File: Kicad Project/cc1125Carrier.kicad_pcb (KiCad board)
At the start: 2 copper layers, 65.9 x 78 mm, 7 parts, among them J1 TFM-110-02-SM-D-A-K-TR, J2 TFM-110-02-SM-D-A-K-TR, J3 Jumper Block, J4 Conn_01x06, U1 YAAJ_WeAct_BlackPill_Part_Lik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

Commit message: add STM project & re-arrange to include it
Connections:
- U1 pad 23: NRST -> unconnected-(U1-Pad23)
- U1 pad 29: unconnected-(U1-Pad29) -> NRST
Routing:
- net NRST: track 45.9 -> 38.1 mm
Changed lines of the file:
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@@
   (net 43 "unconnected-(U1-Pad9)")
   (net 44 "unconnected-(U1-Pad10)")
-  (net 45 "unconnected-(U1-Pad29)")
+  (net 45 "unconnected-(U1-Pad23)")
   (net 46 "unconnected-(U1-Pad16)")
   (net 47 "unconnected-(U1-Pad24)")
@@
       (net 50 "unconnected-(U1-Pad22)") (pinfunction "PC13") (pintype "bidirectional"))
     (pad "23" thru_hole circle locked (at 15.24 43.18 90) (size 1.7 1.7) (drill 1) (layers *.Cu *.Mask)
-      (net 21 "NRST") (pinfunction "PC14") (pintype "bidirectional"))
+      (net 45 "unconnected-(U1-Pad23)") (pinfunction "PC14") (pintype "bidirectional"))
     (pad "24" thru_hole circle locked (at 15.24 40.64 90) (size 1.7 1.7) (drill 1) (layers *.Cu *.Mask)
       (net 47 "unconnected-(U1-Pad24)") (pinfunction "PC15") (pintype "bidirectional"))
@@
       (net 10 "GPIO0") (pinfunction "PA2") (pintype "bidirectional"))
     (pad "29" thru_hole circle locked (at 15.24 27.94 90) (size 1.7 1.7) (drill 1) (layers *.Cu *.Mask)
-      (net 45 "unconnected-(U1-Pad29)") (pinfunction "PA3") (pintype "bidirectional"))
+      (net 21 "NRST") (pinfunction "PA3") (pintype "bidirectional"))
     (pad "30" thru_hole circle locked (at 15.24 25.4 90) (size 1.7 1.7) (drill 1) (layers *.Cu *.Mask)
       (net 14 "NSS") (pinfunction "PA4") (pintype "bidirectional"))
@@
   (segment (start 125 94.72) (end 125.005 94.725) (width 0.25) (layer "F.Cu") (net 21))
   (via (at 125 94.72) (size 0.8) (drill 0.4) (layers "F.Cu" "B.Cu") (net 21))
-  (segment (start 140.39 97.73) (end 136.75 94.09) (width 0.25) (layer "B.Cu") (net 21))
-  (segment (start 125.63 94.09) (end 125 94.72) (width 0.25) (layer "B.Cu") (net 21))
-  (segment (start 136.75 94.09) (end 125.63 94.09) (width 0.25) (layer "B.Cu") (net 21))
-  (segment (start 140.39 113.19) (end 140.39 97.73) (width 0.25) (layer "B.Cu") (net 21))
-  (segment (start 133.76 119.82) (end 140.39 113.19) (width 0.25) (layer "B.Cu") (net 21))
+  (segment (start 116.74 102.98) (end 125 94.72) (width 0.25) (layer "B.Cu") (net 21))
+  (segment (start 121.001988 108.18) (end 116.97 108.18) (width 0.25) (layer "B.Cu") (net 21))
+  (segment (start 118.52 119.82) (end 118.52 114.69) (width 0.25) (layer "B.Cu") (net 21))
+  (segment (start 121.659511 108.837523) (end 121.001988 108.18) (width 0.25) (layer "B.Cu") (net 21))
+  (segment (start 116.74 107.95) (end 116.74 102.98) (width 0.25) (layer "B.Cu") (net 21))
+  (segment (start 118.52 114.69) (end 121.659511 111.550489) (width 0.25) (layer "B.Cu") (net 21))
+  (segment (start 121.659511 111.550489) (end 121.659511 108.837523) (width 0.25) (layer "B.Cu") (net 21))
+  (segment (start 116.97 108.18) (end 116.74 107.95) (width 0.25) (layer "B.Cu") (net 21))
   (segment (start 117.945 109.515) (end 114.87 112.59) (width 0.25) (layer "B.Cu") (net 28))
   (segment (start 109.54 117.92) (end 109.54 117.31) (width 0.25) (layer "B.Cu") (net 28))

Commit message: move signals off of PA0 and PB2 due to conflict with stm32 buttons
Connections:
- U1 pad 12: unconnected-(U1-Pad12) -> GPIO2
- U1 pad 26: GPIO2 -> unconnected-(U1-Pad26)
- U1 pad 36: GPIO_OUT_1 -> unconnected-(U1-Pad36)
- U1 pad 4: unconnected-(U1-Pad4) -> GPIO_OUT_1
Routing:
- net GPIO2: track 12.2 -> 31.3 mm, vias 0 -> 2
- net GPIO_OUT_1: track 14.3 -> 31.4 mm, vias 0 -> 2
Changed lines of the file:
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@@
   (net 38 "unconnected-(U1-Pad2)")
   (net 39 "unconnected-(U1-Pad3)")
-  (net 40 "unconnected-(U1-Pad4)")
+  (net 40 "unconnected-(U1-Pad26)")
   (net 41 "unconnected-(U1-Pad5)")
   (net 42 "unconnected-(U1-Pad8)")
@@
   (net 56 "unconnected-(U1-Pad44)")
   (net 57 "unconnected-(U1-Pad11)")
-  (net 58 "unconnected-(U1-Pad12)")
+  (net 58 "unconnected-(U1-Pad36)")
   (net 59 "unconnected-(U1-Pad13)")
   (net 60 "Net-(J1-Pad10)")
@@
       (net 39 "unconnected-(U1-Pad3)") (pinfunction "PB14") (pintype "bidirectional"))
     (pad "4" thru_hole circle locked (at 0 7.62 90) (size 1.7 1.7) (drill 1) (layers *.Cu *.Mask)
-      (net 40 "unconnected-(U1-Pad4)") (pinfunction "PB15") (pintype "bidirectional"))
+      (net 72 "GPIO_OUT_1") (pinfunction "PB15") (pintype "bidirectional"))
     (pad "5" thru_hole circle locked (at 0 10.16 90) (size 1.7 1.7) (drill 1) (layers *.Cu *.Mask)
       (net 41 "unconnected-(U1-Pad5)") (pinfunction "PA8") (pintype "bidirectional"))
@@
       (net 57 "unconnected-(U1-Pad11)") (pinfunction "PB3") (pintype "bidirectional"))
     (pad "12" thru_hole circle locked (at 0 27.94 90) (size 1.7 1.7) (drill 1) (layers *.Cu *.Mask)
-      (net 58 "unconnected-(U1-Pad12)") (pinfunction "PB4") (pintype "bidirectional"))
+      (net 12 "GPIO2") (pinfunction "PB4") (pintype "bidirectional"))
     (pad "13" thru_hole circle locked (at 0 30.48 90) (size 1.7 1.7) (drill 1) (layers *.Cu *.Mask)
       (net 59 "unconnected-(U1-Pad13)") (pinfunction "PB5") (pintype "bidirectional"))
@@
       (net 49 "unconnected-(U1-Pad25)") (pinfunction "RES") (pintype "input"))
     (pad "26" thru_hole circle locked (at 15.24 35.56 90) (size 1.7 1.7) (drill 1) (layers *.Cu *.Mask)
-      (net 12 "GPIO2") (pinfunction "PA0") (pintype "bidirectional"))
+      (net 40 "unconnected-(U1-Pad26)") (pinfunction "PA0") (pintype "bidirectional"))
     (pad "27" thru_hole circle locked (at 15.24 33.02 90) (size 1.7 1.7) (drill 1) (layers *.Cu *.Mask)
       (net 28 "GPIO3") (pinfunction "PA1") (pintype "bidirectional"))
@@
       (net 73 "GPIO_OUT_2") (pinfunction "PB1") (pintype "bidirectional"))
     (pad "36" thru_hole circle locked (at 15.24 10.16 90) (size 1.7 1.7) (drill 1) (layers *.Cu *.Mask)
-      (net 72 "GPIO_OUT_1") (pinfunction "PB2") (pintype "bidirectional"))
+      (net 58 "unconnected-(U1-Pad36)") (pinfunction "PB2") (pintype "bidirectional"))
     (pad "37" thru_hole circle locked (at 15.24 7.62 90) (size 1.7 1.7) (drill 1) (layers *.Cu *.Mask)
       (net 75 "unconnected-(U1-Pad37)") (pinfunction "PB10") (pintype "bidirectional"))
@@
   (segment (start 128.17 114.53) (end 133.185 109.515) (width 0.25) (layer "B.Cu") (net 10))
   (segment (start 126.35 114.53) (end 128.17 114.53) (width 0.25) (layer "B.Cu") (net 10))
-  (segment (start 130.645 113.615) (end 130.645 109.515) (width 0.25) (layer "F.Cu") (net 12))
-  (segment (start 126.14 118.12) (end 130.645 113.615) (width 0.25) (layer "F.Cu") (net 12))
-  (segment (start 126.14 119.82) (end 126.14 118.12) (width 0.25) (layer "F.Cu") (net 12))
+  (segment (start 124.04 129.54) (end 118.52 135.06) (width 0.25) (layer "F.Cu") (net 12))
+  (segment (start 130.645 109.515) (end 129.854511 110.305489) (width 0.25) (layer "F.Cu") (net 12))
+  (segment (start 124.04 128.54) (end 124.04 129.54) (width 0.25) (layer "F.Cu") (net 12))
+  (segment (start 129.854511 110.305489) (end 129.854511 120.306499) (width 0.25) (layer "F.Cu") (net 12))
+  (segment (start 129.854511 120.306499) (end 126.08101 124.08) (width 0.25) (layer "F.Cu") (net 12))
+  (segment (start 126.08101 124.08) (end 124.91 124.08) (width 0.25) (layer "F.Cu") (net 12))
+  (segment (start 124.055 124.935) (end 124.03 124.96) (width 0.25) (layer "F.Cu") (net 12))
+  (segment (start 124.91 124.08) (end 124.055 124.935) (width 0.25) (layer "F.Cu") (net 12))
+  (via (at 124.04 128.54) (size 0.8) (drill 0.4) (layers "F.Cu" "B.Cu") (net 12))
+  (via (at 124.055 124.935) (size 0.8) (drill 0.4) (layers "F.Cu" "B.Cu") (net 12))
+  (segment (start 124.055 128.525) (end 124.04 128.54) (width 0.25) (layer "B.Cu") (net 12))
+  (segment (start 124.055 124.935) (end 124.055 128.525) (width 0.25) (layer "B.Cu") (net 12))
   (segment (start 119.13 116.64) (end 120.98 116.64) (width 0.25) (layer "F.Cu") (net 14))
   (segment (start 117.154511 118.615489) (end 119.13 116.64) (width 0.25) (layer "F.Cu") (net 14))
@@
   (segment (start 126.55 101.46) (end 127.81 100.2) (width 0.25) (layer "B.Cu") (net 66))
   (segment (start 117.945 106.975) (end 123.46 101.46) (width 0.25) (layer "B.Cu") (net 66))
+  (segment (start 98.2 128) (end 98.2 135.06) (width 0.25) (layer "F.Cu") (net 72))
+  (segment (start 102.105489 124.084511) (end 101.55 124.64) (width 0.25) (layer "F.Cu") (net 72))
+  (segment (start 101.55 124.64) (end 101.47 124.72) (width 0.25) (layer "F.Cu") (net 72))
+  (segment (start 99.02 127.18) (end 98.2 128) (width 0.25) (layer "F.Cu") (net 72))
   (segment (start 110.325 110.235) (end 110.325 109.515) (width 0.25) (layer "F.Cu") (net 72))
-  (segment (start 100.74 119.82) (end 110.325 110.235) (width 0.25) (layer "F.Cu") (net 72))
+  (segment (start 102.105489 117.734511) (end 102.105489 124.084511) (width 0.25) (layer "F.Cu") (net 72))
+  (segment (start 110.325 109.515) (end 102.105489 117.734511) (width 0.25) (layer "F.Cu") (net 72))
+  (via (at 101.55 124.64) (size 0.8) (drill 0.4) (layers "F.Cu" "B.Cu") (net 72))
+  (via (at 99.02 127.18) (size 0.8) (drill 0.4) (layers "F.Cu" "B.Cu") (net 72))
+  (segment (start 101.55 124.64) (end 99.02 127.17) (width 0.25) (layer "B.Cu") (net 72))
+  (segment (start 99.02 127.17) (end 99.02 127.18) (width 0.25) (layer "B.Cu") (net 72))
   (segment (start 103.28 119.82) (end 112.865 110.235) (width 0.25) (layer "F.Cu") (net 73))
   (segment (start 112.865 110.235) (end 112.865 109.515) (width 0.25) (layer "F.Cu") (net 73))
@@
     (connect_pads (clearance 0.508))
     (min_thickness 0.254) (filled_areas_thickness no)
-    (fill yes (thermal_gap 0.508) (thermal_bridge_width 0.508))
+    (fill (thermal_gap 0.508) (thermal_bridge_width 0.508))
     (polygon
       (pts

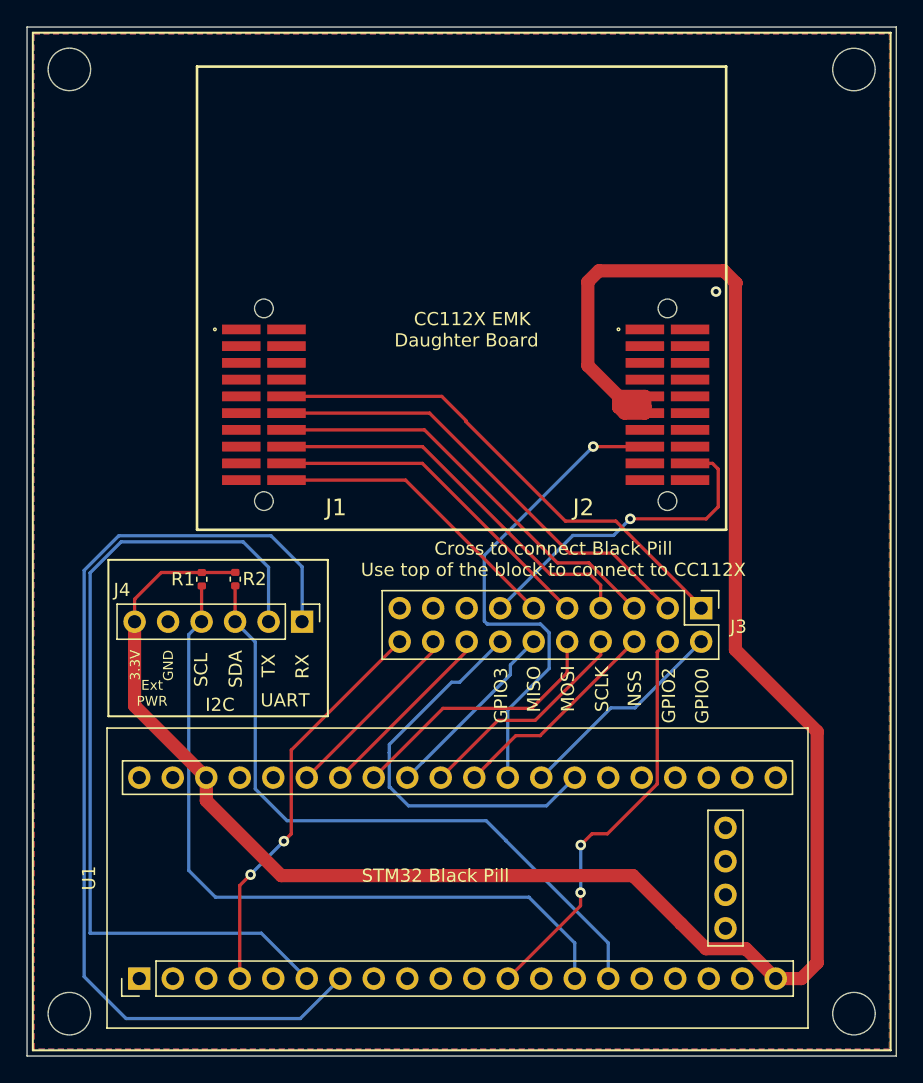
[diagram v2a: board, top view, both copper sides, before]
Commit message: tweak cc1125 footprint
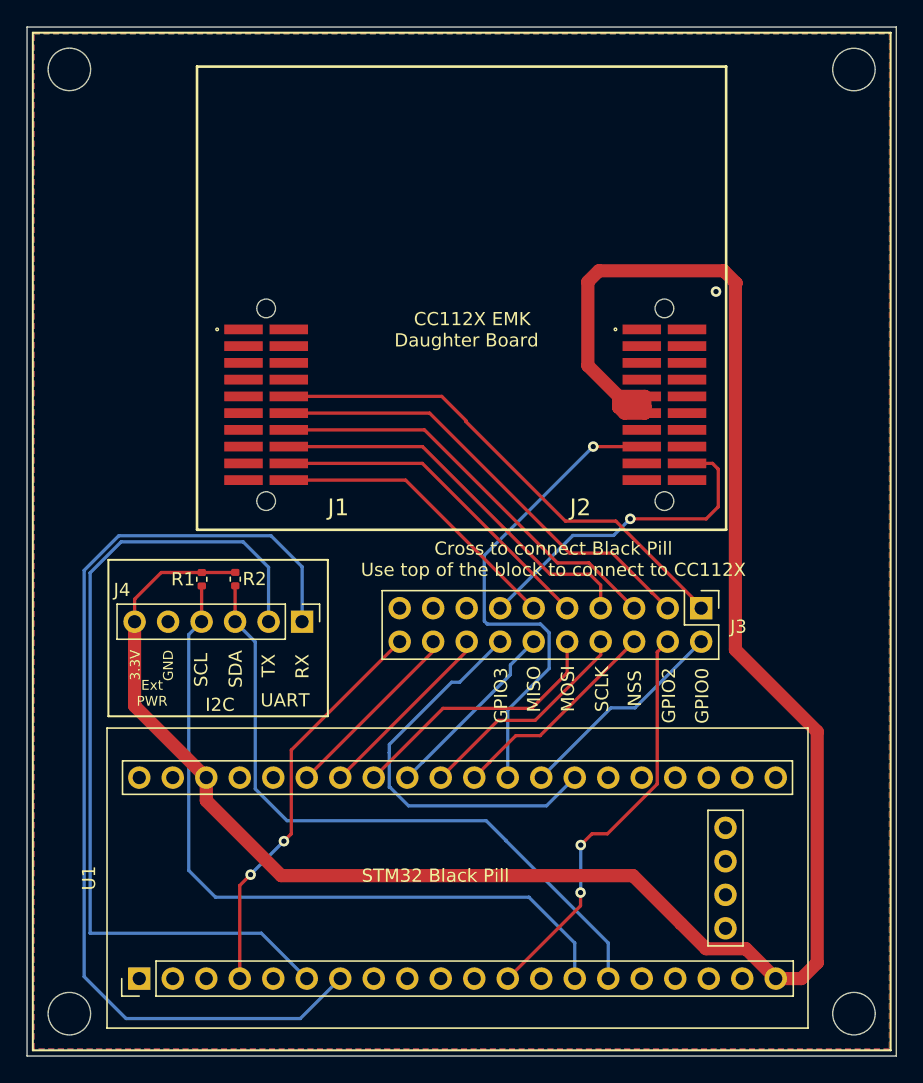
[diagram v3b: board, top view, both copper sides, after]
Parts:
- moved J2 0.23 mm to (130.4, 91.5)
- moved J1 0.17 mm to (100.2, 91.5)
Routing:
- net GPIO_OUT_1: track 31.4 -> 30.6 mm
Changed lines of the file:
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@@
   )
   (footprint "SamacSys_Parts:TFM-110-02-XXX-D-A-Y-TR" (layer "F.Cu")
-    (at 100.03 91.55 -90)
+    (at 100.2 91.55 -90)
     (descr "TFM-110-02-XXX-D-A-Y-TR")
     (tags "Connector")
@@
   )
   (footprint "SamacSys_Parts:TFM-110-02-XXX-D-A-Y-TR" (layer "F.Cu")
-    (at 130.63 91.55 -90)
+    (at 130.4 91.55 -90)
     (descr "TFM-110-02-XXX-D-A-Y-TR")
     (tags "Connector")
@@
   (segment (start 129.854511 120.306499) (end 126.08101 124.08) (width 0.25) (layer "F.Cu") (net 12))
   (segment (start 126.08101 124.08) (end 124.91 124.08) (width 0.25) (layer "F.Cu") (net 12))
-  (segment (start 124.055 124.935) (end 124.03 124.96) (width 0.25) (layer "F.Cu") (net 12))
   (segment (start 124.91 124.08) (end 124.055 124.935) (width 0.25) (layer "F.Cu") (net 12))
   (via (at 124.04 128.54) (size 0.8) (drill 0.4) (layers "F.Cu" "B.Cu") (net 12))
@@
   (segment (start 98.2 128) (end 98.2 135.06) (width 0.25) (layer "F.Cu") (net 72))
   (segment (start 102.105489 124.084511) (end 101.55 124.64) (width 0.25) (layer "F.Cu") (net 72))
-  (segment (start 101.55 124.64) (end 101.47 124.72) (width 0.25) (layer "F.Cu") (net 72))
   (segment (start 99.02 127.18) (end 98.2 128) (width 0.25) (layer "F.Cu") (net 72))
-  (segment (start 110.325 110.235) (end 110.325 109.515) (width 0.25) (layer "F.Cu") (net 72))
   (segment (start 102.105489 117.734511) (end 102.105489 124.084511) (width 0.25) (layer "F.Cu") (net 72))
   (segment (start 110.325 109.515) (end 102.105489 117.734511) (width 0.25) (layer "F.Cu") (net 72))
@@
     (connect_pads (clearance 0.508))
     (min_thickness 0.254) (filled_areas_thickness no)
-    (fill (thermal_gap 0.508) (thermal_bridge_width 0.508))
+    (fill yes (thermal_gap 0.508) (thermal_bridge_width 0.508))
     (polygon
       (pts
@@
     )
   )
-  (group "" (id a6fa195f-5878-4102-b046-6062db6dbec9)
+  (group "" (id 1f4b2627-9d4b-41f1-94a4-032cc7b2202f)
     (members
       1b63546f-1a57-47bf-b4ee-8505e232c513

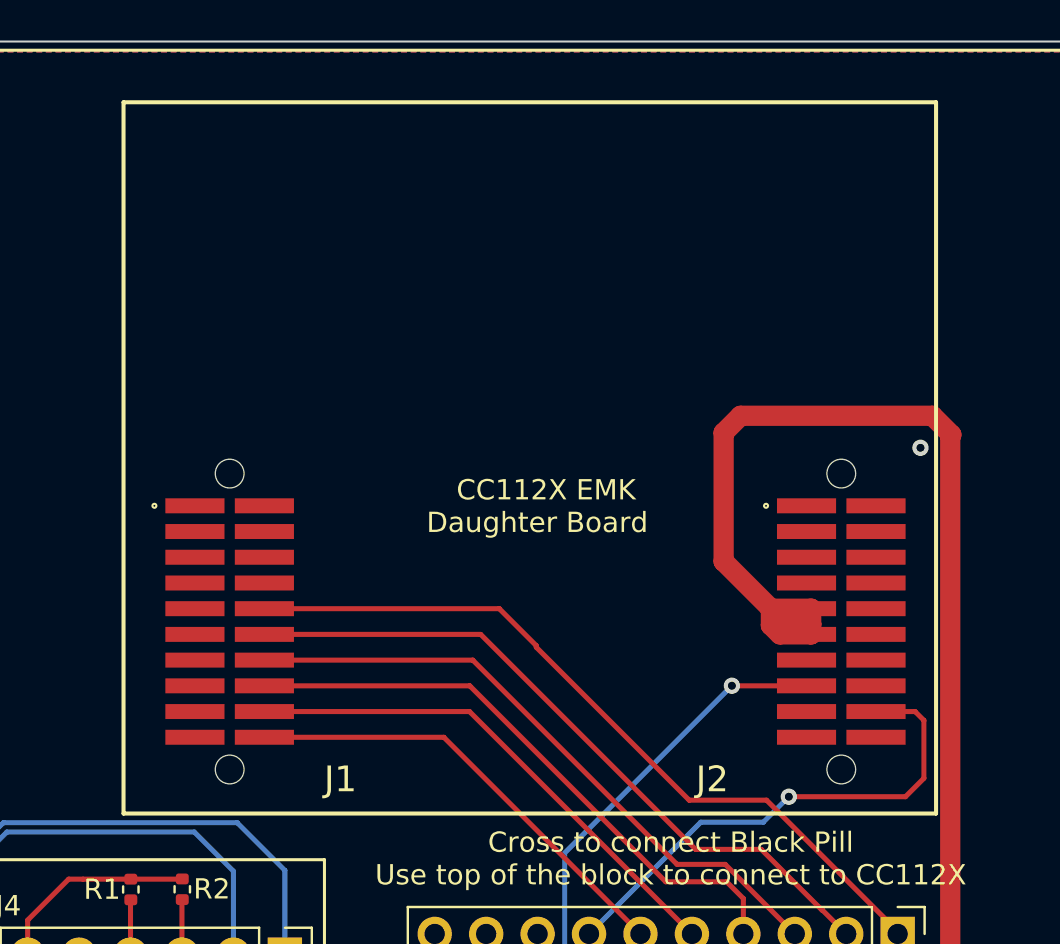
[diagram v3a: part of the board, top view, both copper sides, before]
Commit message: add emk daughter board symbol and footprint
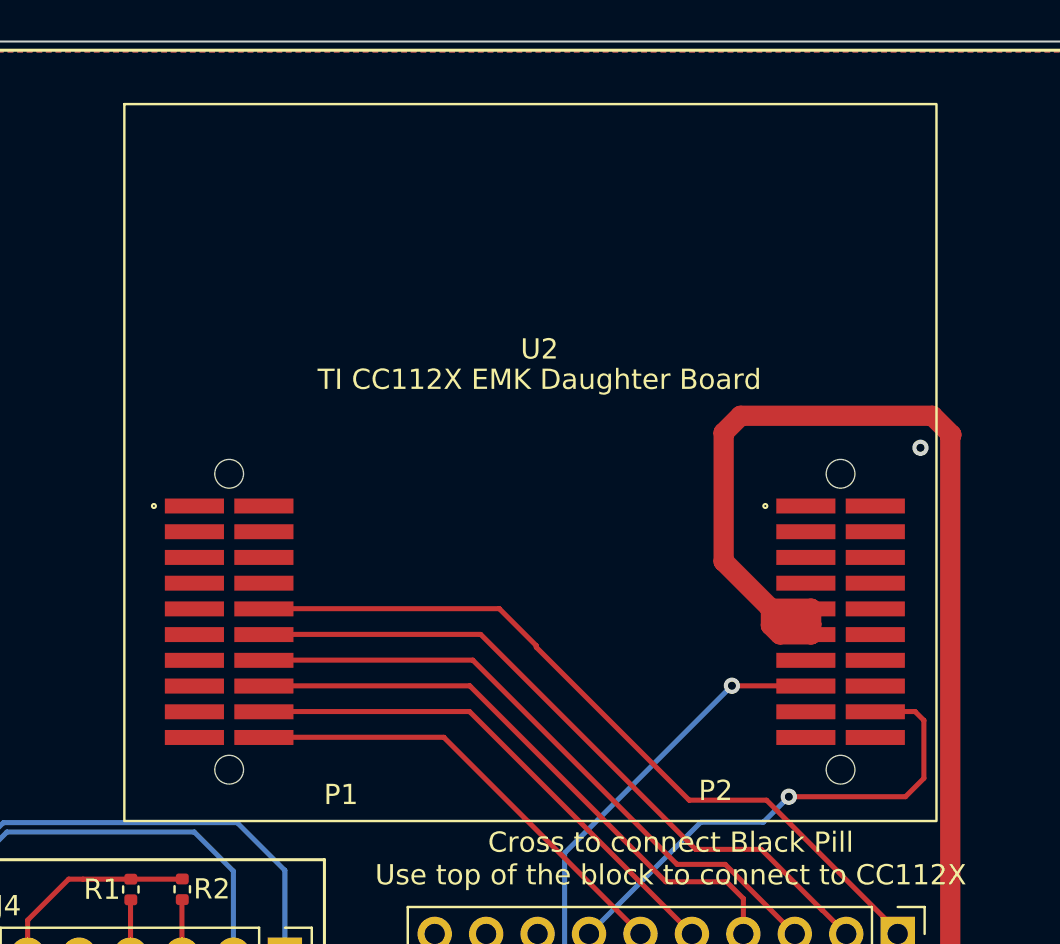
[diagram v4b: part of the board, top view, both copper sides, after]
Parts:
- removed J1, J2: TFM-110-02-SM-D-A-K-TR, SamacSys_Parts:TFM-110-02-XXX-D-A-Y-TR
- added U2: TI CC112X EMK Daughter Board, RF:CC112XEMK, F.Cu at (115.3, 82.4)
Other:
- board text removed: "CC112X EMK Daughter Board"
